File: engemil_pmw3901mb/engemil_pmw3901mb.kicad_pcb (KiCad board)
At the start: 2 copper layers, 50 x 30 mm, 20 parts, among them J1 6130XX11121, U1 PMW3901MB-TXQT, U2 TPD8E003DQDR, U3 LM66100QDCKRQ1, U4 TLV77318PDBVR

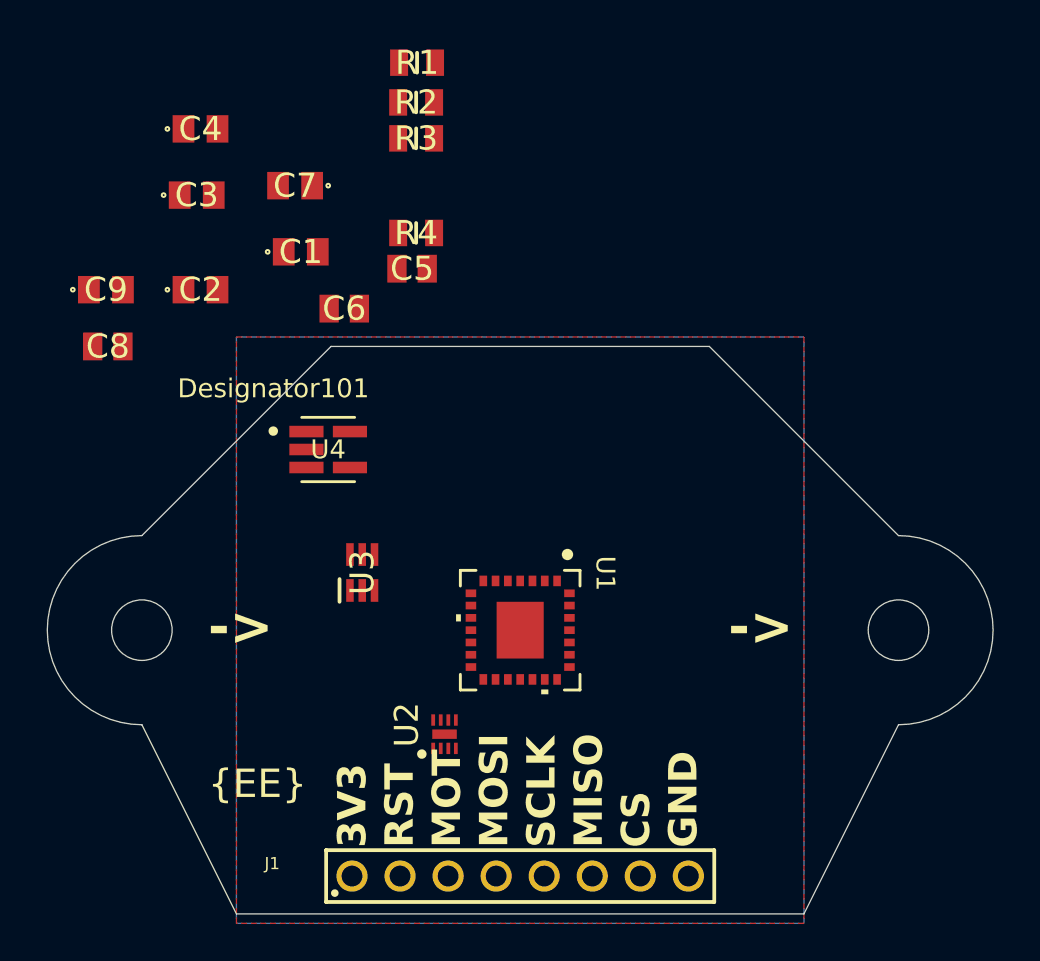
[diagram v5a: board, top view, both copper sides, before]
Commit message: - Finalized version 2 - Updated PCB pdf file - Updated README - Updated images - Updated PCB design - Updated gerber files
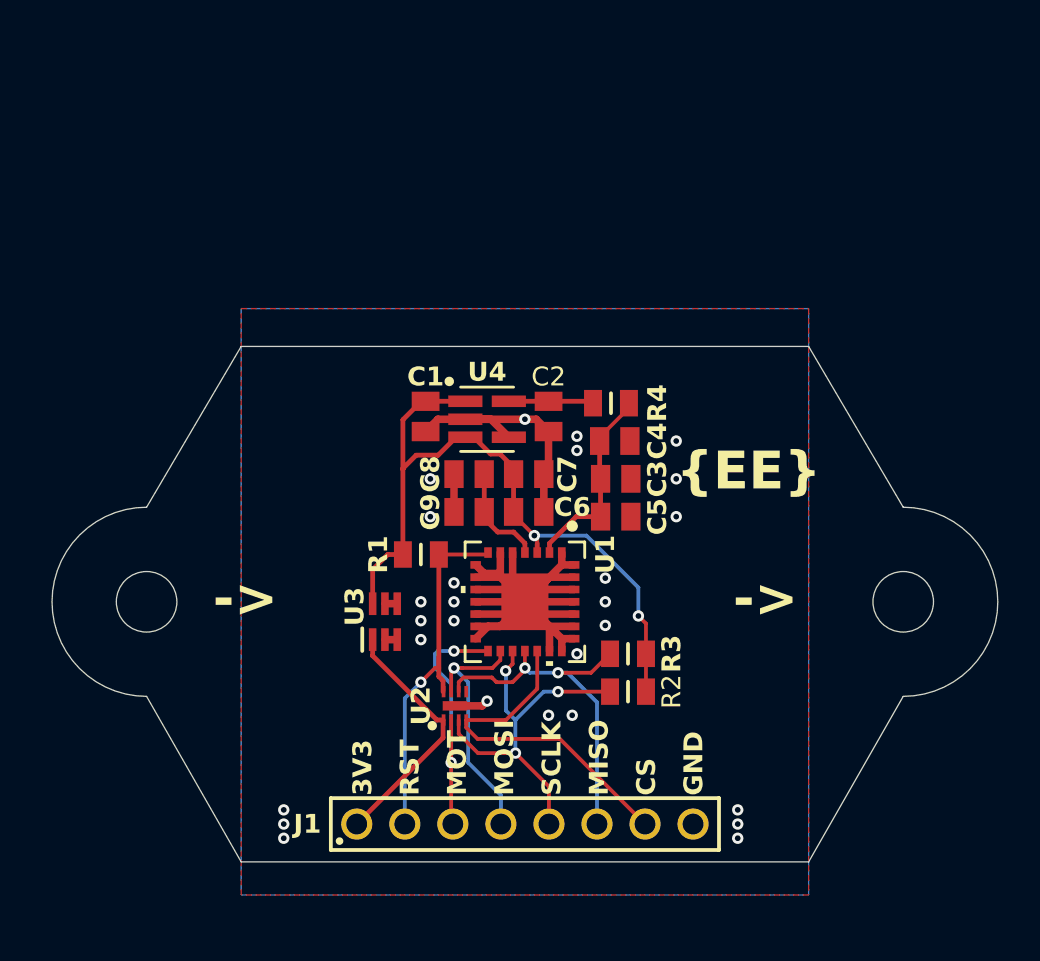
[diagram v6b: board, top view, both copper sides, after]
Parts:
- C1, C2, C3, C4, C7, C9: footprint engemil_pmw3901mb_module_footprint_library:C0805 -> engemil_pmw3901mb_module_footprint_library:CAPC2012X110N
- moved R2 33.1 mm to (155.7, 118.2), turned to 180 degrees
- moved R3 29.5 mm to (155.7, 116.2), turned to 180 degrees
- moved C4 27.4 mm to (155.0, 105.0)
- moved C3 26.8 mm to (155.1, 107.0)
- moved R1 26.0 mm to (144.8, 111.0)
- moved C9 22.5 mm to (147.3, 108.8), turned to 180 degrees
- moved C8 20.3 mm to (147.3, 106.8), turned to 180 degrees
- moved C7 19.6 mm to (150.4, 106.8), turned to 0 degrees
- moved C2 19.6 mm to (151.5, 103.7), turned to 90 degrees
- moved C5 17.0 mm to (155.1, 109.0)
- moved C6 14.5 mm to (150.4, 108.8)
- moved R4 13.7 mm to (154.8, 103.0)
- moved C1 10.9 mm to (145.0, 103.7), turned to 90 degrees
- moved U4 8.55 mm to (148.2, 103.9)
- moved U3 2.86 mm to (142.8, 114.5)
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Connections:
- U1 pad 1: Net-(U1-GND-Pad1) -> GND
- U1 pad 20: Net-(U1-GND-Pad1) -> GND
- U1 pad 21: Net-(U1-GND-Pad1) -> GND
- U1 pad 22: Net-(U1-GND-Pad1) -> GND
- U1 pad 23: Net-(U1-GND-Pad1) -> GND
- U1 pad 24: Net-(U1-GND-Pad1) -> GND
- U1 pad 25: Net-(U1-GND-Pad1) -> GND
- U1 pad 26: Net-(U1-GND-Pad1) -> GND
- U1 pad 27: Net-(U1-GND-Pad1) -> GND
- U1 pad 28: Net-(U1-GND-Pad1) -> GND
- U1 pad 29: Net-(U1-GND-Pad1) -> GND
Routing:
- net GND: track 0.00 -> 64.2 mm, vias 0 -> 27
- net +3.3V: track 0.00 -> 39.5 mm, vias 0 -> 2
- net SCLK: track 0.00 -> 20.1 mm, vias 0 -> 3
- net MISO: track 0.00 -> 19.6 mm, vias 0 -> 2
- net RESET: track 0.00 -> 19.1 mm, vias 0 -> 1
- net CS: track 0.00 -> 18.4 mm
- net MOTION: track 0.00 -> 14.6 mm, vias 0 -> 2
- net MOSI: track 0.00 -> 13.7 mm, vias 0 -> 1
- net VCC: track 0.00 -> 13.4 mm
- net Net-(U1-VDD): track 0.00 -> 10.4 mm
- net Net-(U1-VREG): track 0.00 -> 5.53 mm
- net +1V8: track 0.00 -> 4.49 mm
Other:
- board size 50 x 30 mm -> 50 x 27.2 mm
- board text added: "Designed by EngEmil.io"
- board text added: "EngEmil PMW3901MB v2.0"
- board text removed: "Designed by EngEmil.io {EE}"
- board text removed: "EngEmil PMW3901MB v1.0"
